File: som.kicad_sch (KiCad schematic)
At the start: 24 parts, among them U201 74LVC2G17GV

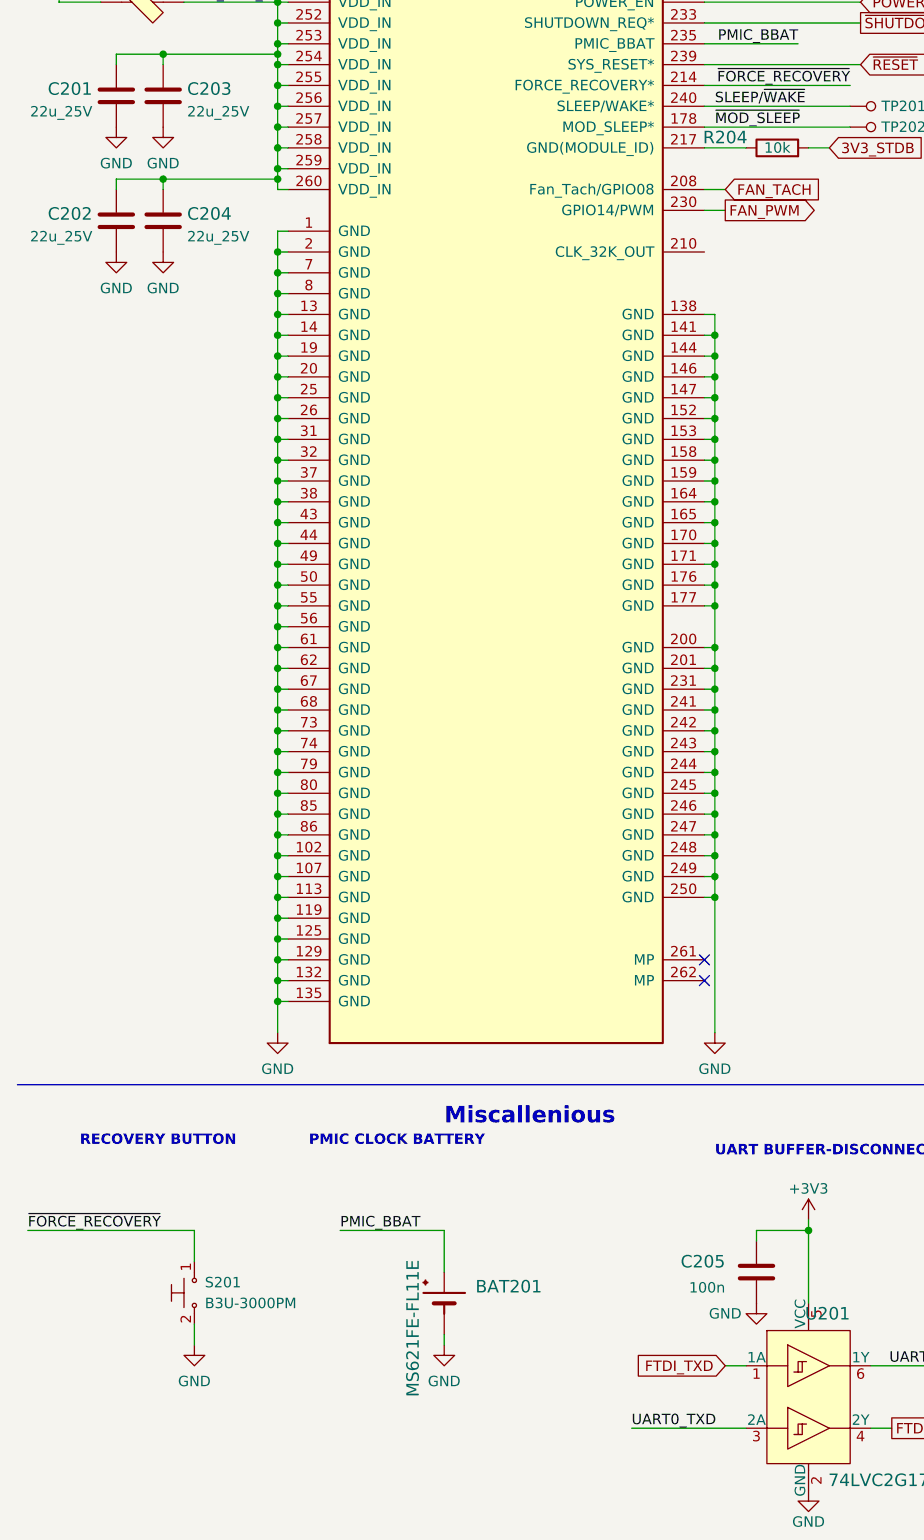
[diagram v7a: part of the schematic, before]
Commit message: Unified schematic look of ethernet sheet, improved shielding of eth connector, replaced gnd symbols
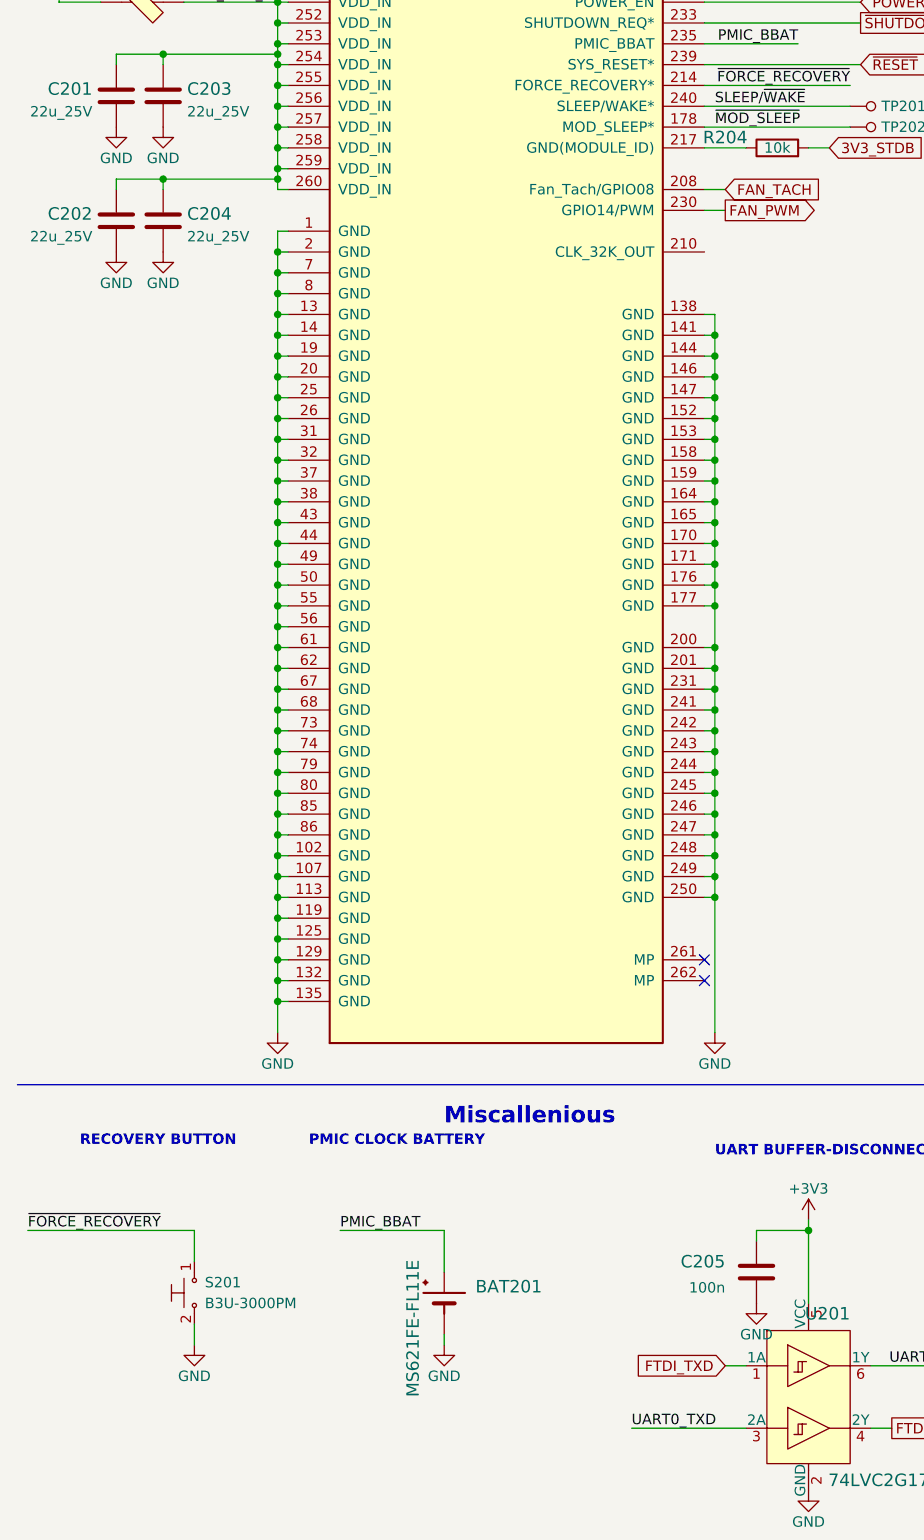
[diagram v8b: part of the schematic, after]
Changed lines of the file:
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@@
       (effects (font (size 1.27 1.27)) hide)
     )
-    (property "Value" "GND" (id 1) (at 24.765 106.0434 0))
+    (property "Value" "GND" (id 1) (at 24.765 105.41 0))
     (property "Footprint" "" (id 2) (at 24.765 101.6 0)
       (effects (font (size 1.27 1.27)) hide)
@@
       (effects (font (size 1.27 1.27)) hide)
     )
-    (property "Value" "GND" (id 1) (at 44.45 216.5334 0))
+    (property "Value" "GND" (id 1) (at 44.45 215.9 0))
     (property "Footprint" "" (id 2) (at 44.45 212.09 0)
       (effects (font (size 1.27 1.27)) hide)
@@
       (effects (font (size 1.27 1.27)) hide)
     )
-    (property "Value" "GND" (id 1) (at 30.48 121.2834 0))
+    (property "Value" "GND" (id 1) (at 30.48 120.65 0))
     (property "Footprint" "" (id 2) (at 30.48 116.84 0)
       (effects (font (size 1.27 1.27)) hide)
@@
       (effects (font (size 1.27 1.27)) hide)
     )
-    (property "Value" "GND" (id 1) (at 64.77 254.6334 0))
+    (property "Value" "GND" (id 1) (at 64.77 254 0))
     (property "Footprint" "" (id 2) (at 64.77 250.19 0)
       (effects (font (size 1.27 1.27)) hide)
@@
       (effects (font (size 1.27 1.27)) hide)
     )
-    (property "Value" "GND" (id 1) (at 24.765 121.2834 0))
+    (property "Value" "GND" (id 1) (at 24.765 120.65 0))
     (property "Footprint" "" (id 2) (at 24.765 116.84 0)
       (effects (font (size 1.27 1.27)) hide)
@@
       (effects (font (size 1.27 1.27)) hide)
     )
-    (property "Value" "GND" (id 1) (at 97.79 216.5334 0))
+    (property "Value" "GND" (id 1) (at 97.79 215.9 0))
     (property "Footprint" "" (id 2) (at 97.79 212.09 0)
       (effects (font (size 1.27 1.27)) hide)
@@
       (effects (font (size 1.27 1.27)) hide)
     )
-    (property "Value" "GND" (id 1) (at 99.06 246.38 0))
+    (property "Value" "GND" (id 1) (at 102.87 248.92 0))
     (property "Footprint" "" (id 2) (at 102.87 245.11 0)
       (effects (font (size 1.27 1.27)) hide)
@@
       (effects (font (size 1.27 1.27)) hide)
     )
-    (property "Value" "GND" (id 1) (at 30.48 106.0434 0))
+    (property "Value" "GND" (id 1) (at 30.48 105.41 0))
     (property "Footprint" "" (id 2) (at 30.48 101.6 0)
       (effects (font (size 1.27 1.27)) hide)
@@
       (effects (font (size 1.27 1.27)) hide)
     )
-    (property "Value" "GND" (id 1) (at 34.29 254.6334 0))
+    (property "Value" "GND" (id 1) (at 34.29 254 0))
     (property "Footprint" "" (id 2) (at 34.29 250.19 0)
       (effects (font (size 1.27 1.27)) hide)
